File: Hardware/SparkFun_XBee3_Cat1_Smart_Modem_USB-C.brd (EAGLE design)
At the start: 53.3 x 59.7 mm, 112 parts, among them J1 USB Female Type C Connector, J3 USB Female Type C Connector, J4 QWIIC_RIGHT_ANGLE, U1 FSUSB30MUX_MSOP10, U2 AP63203, U3 ESD Diode, U5 ESD Diode, U6 CP210X

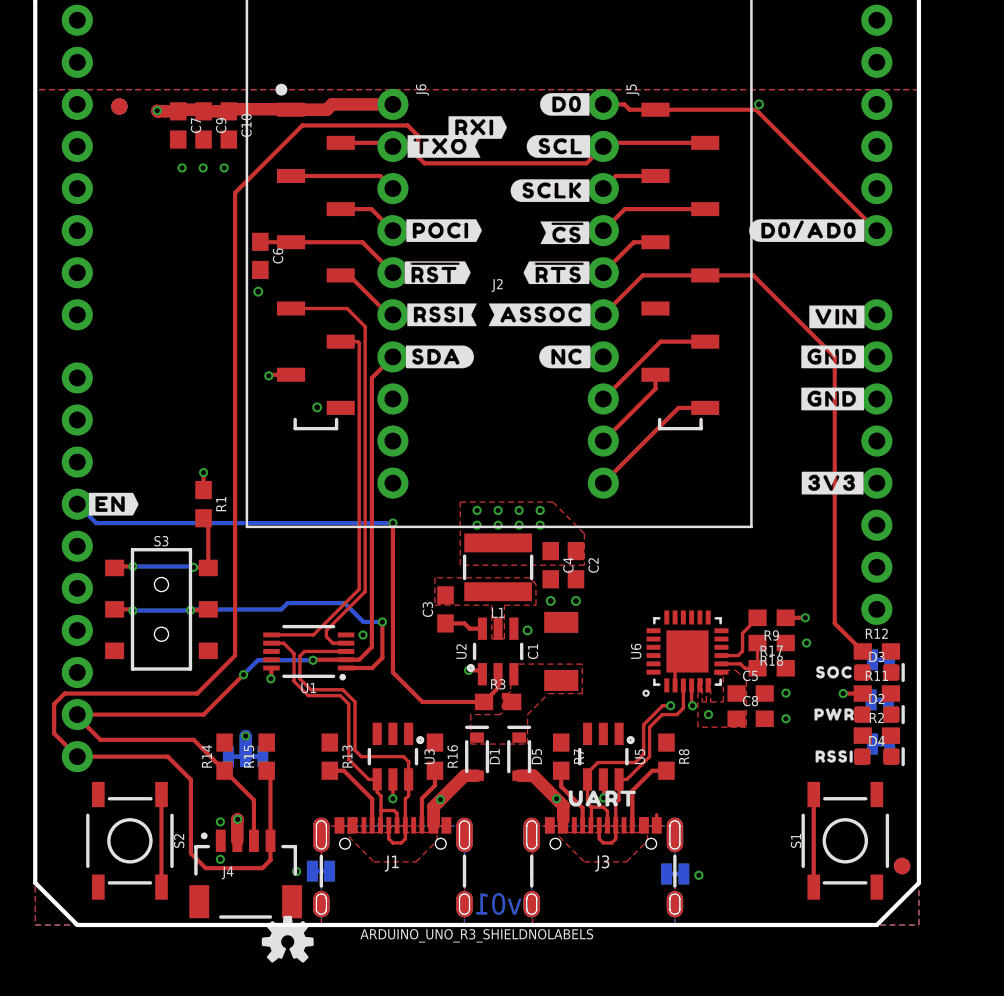
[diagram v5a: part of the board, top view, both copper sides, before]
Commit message: Routes stuff in a sloppy manner - getting rid of airwires
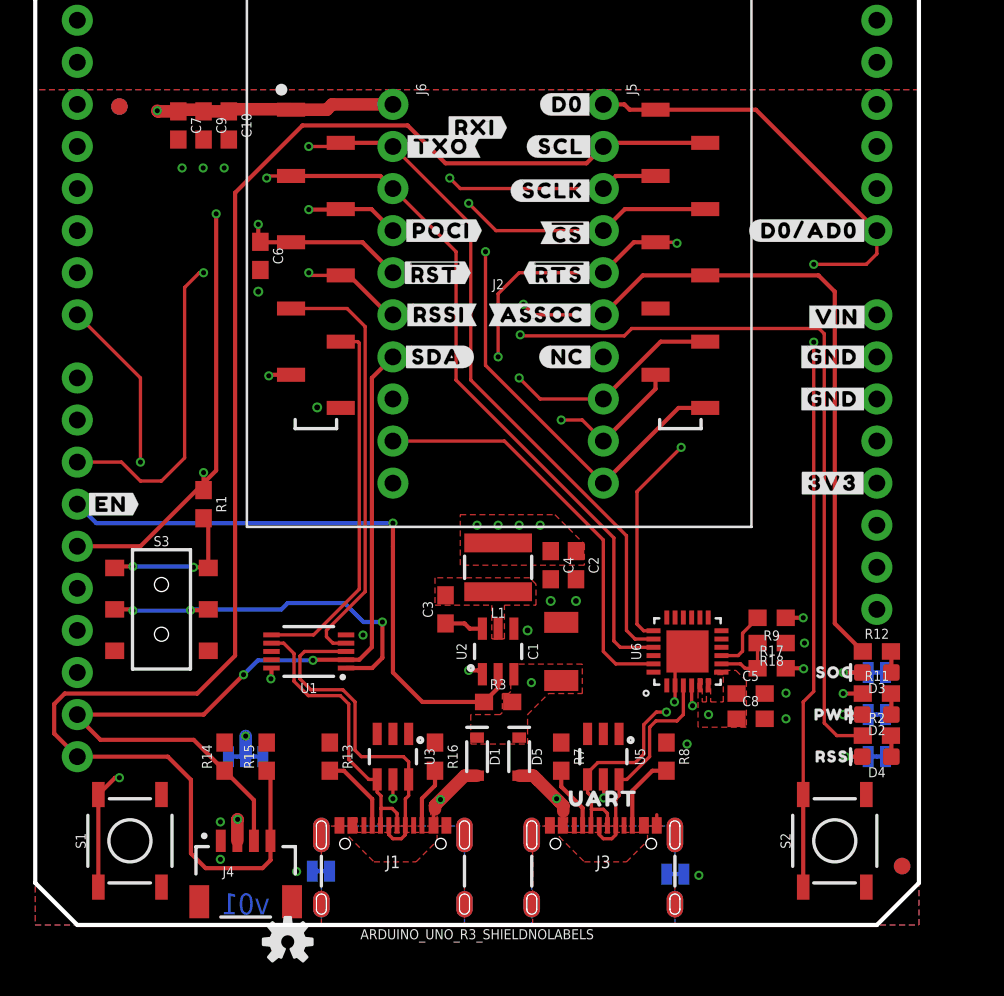
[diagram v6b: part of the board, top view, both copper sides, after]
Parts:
- moved S1 43.2 mm to (5.71, 5.08)
- moved S2 42.5 mm to (48.3, 5.08), turned to 90 degrees
- moved PLED 0.91 mm to (50.8, 12.7), turned to 0 degrees
- moved RLED 0.80 mm to (50.8, 10.2), turned to 0 degrees
- moved ALED 0.80 mm to (50.8, 15.2), turned to 0 degrees
- turned D2 to 180 degrees
- turned D3 to 180 degrees
- turned D4 to 180 degrees
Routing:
- net D10/RSSI_PWM: track 4.14 -> 84.4 mm, vias 0 -> 3
- net D6/!RTS!: track 3.91 -> 68.8 mm, vias 0 -> 3
- net D13/TXO: track 3.55 -> 62.6 mm, vias 0 -> 1
- net D14/RXI: track 6.46 -> 61.0 mm, vias 0 -> 1
- net VIN: track 0.00 -> 51.7 mm, vias 0 -> 2
- net !RESET!: track 14.4 -> 58.0 mm, vias 0 -> 2
- net D4/SPI_PICO: track 8.03 -> 51.3 mm, vias 0 -> 1
- net D7/!CTS!: track 5.30 -> 46.0 mm, vias 0 -> 2
- net D0: track 25.3 -> 63.0 mm, vias 0 -> 2
- net D9/!SLEEP!: track 7.58 -> 44.5 mm, vias 0 -> 1
- net D5/ASSOCIATE: track 36.2 -> 72.4 mm, vias 0 -> 1
- net D2/SPI_CLK: track 3.46 -> 38.4 mm, vias 0 -> 1
- net D3/SPI_!CS!: track 6.69 -> 40.5 mm, vias 0 -> 1
- net D12/SPI_POCI: track 3.69 -> 37.1 mm, vias 0 -> 2
- net D8/!DTR!: track 22.3 -> 47.6 mm
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
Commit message: Routes air wires
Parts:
- moved R1 1.27 mm to (10.2, 24.1)
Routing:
- net VIN: track 51.7 -> 46.3 mm
- net D13/TXO: track 62.6 -> 67.0 mm
- net D14/RXI: track 61.0 -> 65.4 mm
- net D7/!CTS!: track 46.0 -> 49.5 mm, vias 2 -> 1
- net D0: track 63.0 -> 65.3 mm
- net D4/SPI_PICO: track 51.3 -> 53.5 mm
- net D10/RSSI_PWM: track 84.4 -> 82.9 mm
- net D9/!SLEEP!: track 44.5 -> 43.1 mm, vias 1 -> 0
- net !RESET!: track 58.0 -> 56.6 mm
- net FIRMWARE: track 8.84 -> 7.57 mm
- net D12/SPI_POCI: track 37.1 -> 36.1 mm
- net D1/SCL: track 98.7 -> 98.0 mm
- net D3/SPI_!CS!: track 40.5 -> 41.2 mm, vias 1 -> 0
- net D8/!DTR!: track 47.6 -> 48.1 mm
- net D5/ASSOCIATE: vias 1 -> 0
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
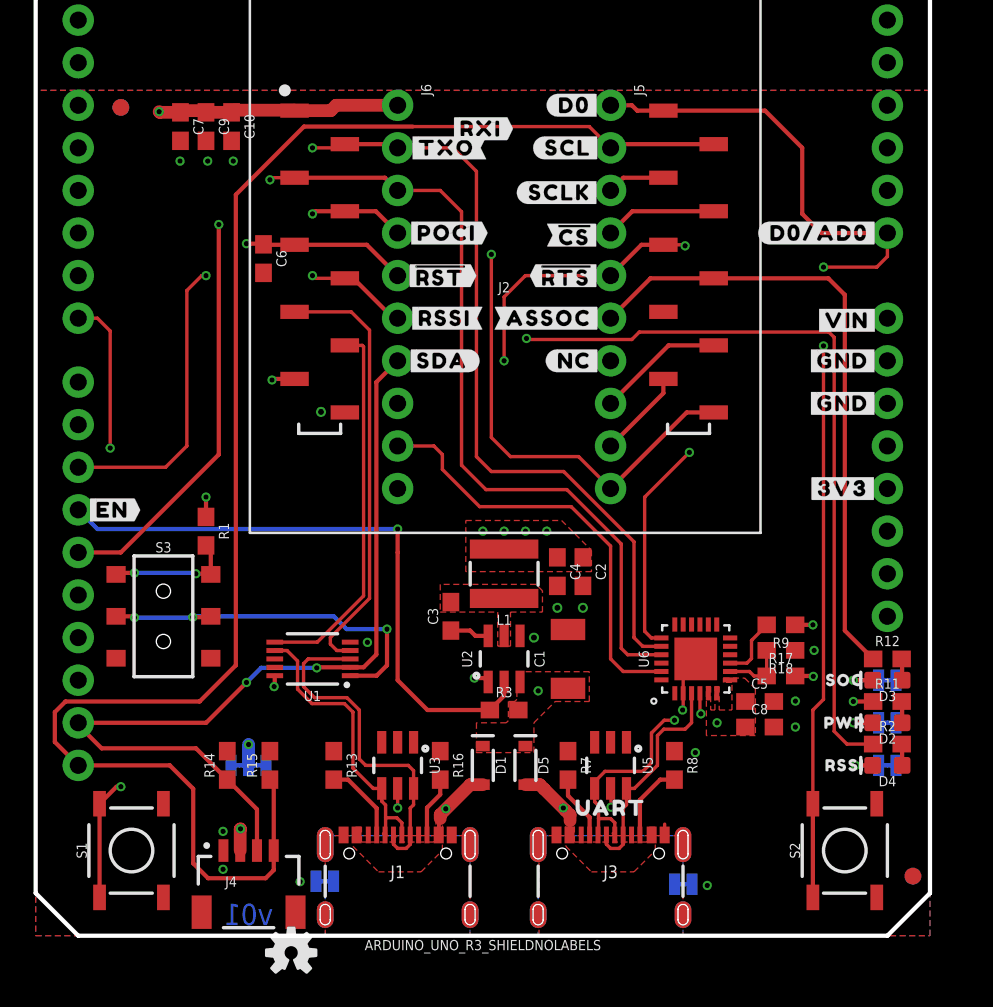
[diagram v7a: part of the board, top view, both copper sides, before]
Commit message: Improves routing spaghetti
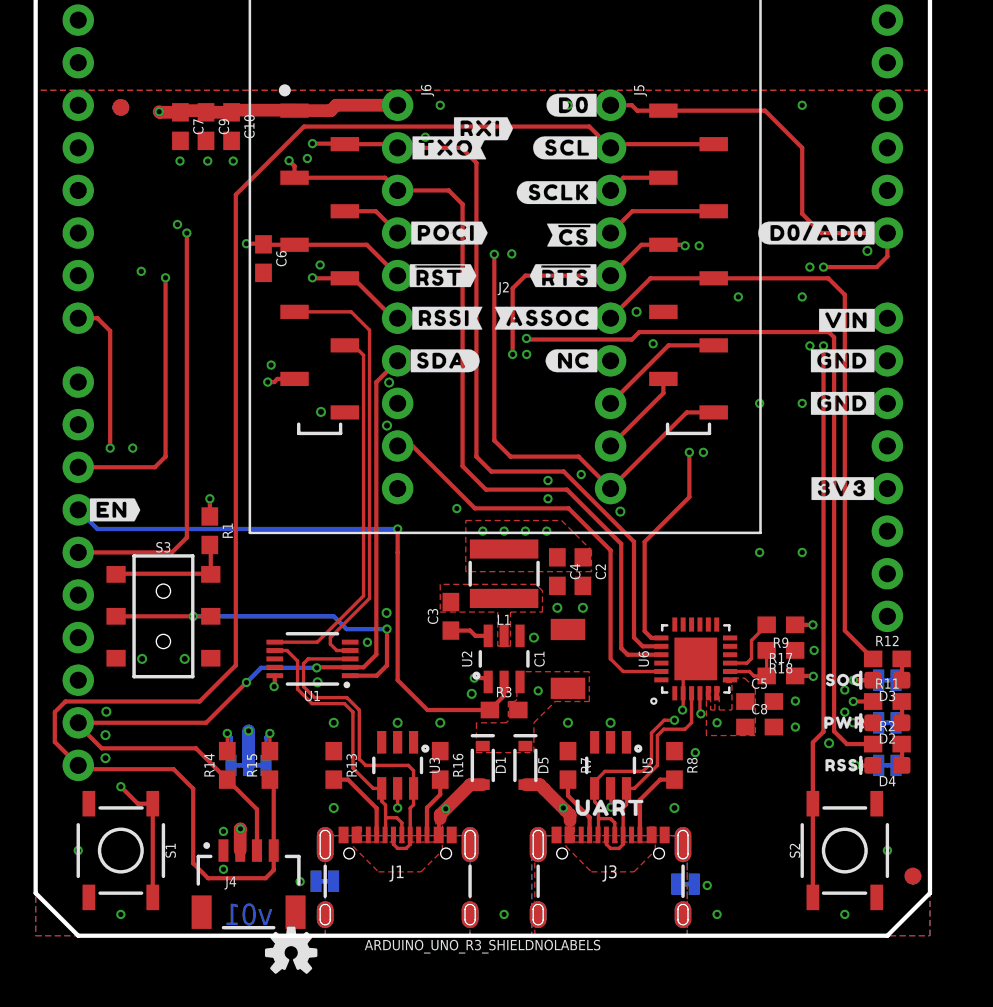
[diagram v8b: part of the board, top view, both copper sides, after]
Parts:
- moved S1 0.63 mm to (5.08, 5.08), turned to 270 degrees
- moved R1 0.23 mm to (10.4, 24.2)
- moved SHLD 0.13 mm to (38.8, 3.07)
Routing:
- net D12/SPI_POCI: track 36.1 -> 41.3 mm, vias 2 -> 1
- net N$13: track 0.00 -> 3.05 mm, vias 0 -> 1
- net N$11: track 0.00 -> 3.05 mm, vias 0 -> 1
- net D10/RSSI_PWM: track 82.9 -> 84.1 mm
- net D14/RXI: track 65.4 -> 64.6 mm
- net D5/ASSOCIATE: track 72.4 -> 71.6 mm
- net D8/!DTR!: track 48.1 -> 47.4 mm
- net GND: track 4.02 -> 3.37 mm, vias 17 -> 73
- net 3.3V: track 31.1 -> 31.7 mm
- net D1/SCL: track 98.0 -> 97.3 mm
- net !RESET!: track 56.6 -> 57.2 mm
- net D3/SPI_!CS!: track 41.2 -> 40.5 mm
- net DIRECT_SELECT: track 22.3 -> 22.2 mm, vias 3 -> 2
- net FIRMWARE: track 7.57 -> 7.63 mm, vias 2 -> 0
